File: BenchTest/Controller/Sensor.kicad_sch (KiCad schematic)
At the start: 1 part, among them J2 Conn_01x03

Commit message: WIP Controller in progress
w
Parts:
- removed J2: Conn_01x03, symbol Connector_Generic:Conn_01x03
- added J2, J4: Conn_01x04, symbol Connector_Generic:Conn_01x04
- added J3: Conn_01x03, symbol Connector_Generic:Conn_01x03
- added R11, R12: 10k, Resistor_SMD:R_0402_1005Metric_Pad0.72x0.64mm_HandSolder, symbol Device:R
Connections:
- net GND: now also J2.3 (Pin_3), J4.4 (Pin_4), R12.2
- net Sense: now also J2.2 (Pin_2)
- new net +5V: J2.4 (Pin_4)
- new net CurentSenseVRef: J2.1 (Pin_1)
- new net PEDAL_OUT: J4.1 (Pin_1), R11.1
- new net PEDAL_SWITCH_0: J4.2 (Pin_2)
- new net PEDAL_SWITCH_1: J4.3 (Pin_3)
- new net Pedal_Signal: R11.2, R12.1
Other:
- note added: "TODO Pedal Connection TODO what is the voltage TODO divide it down? TODO use op-amp for faster slew?"
- note added: "TODO Pedal This signal goes to 3 different controllers. Howdo."
- note added: "TODO expected ~25mA. Switch?"
- note added: "TODO need 2.5V Reference, but able to supply 5mA. Need an LDO here TODO halve Sense? Sensor is hass-200"
- note added: "TODO thermal from motor"
- note removed: "TODO Pinout TODO what is the drive from the current sensor TODO what is the voltage"

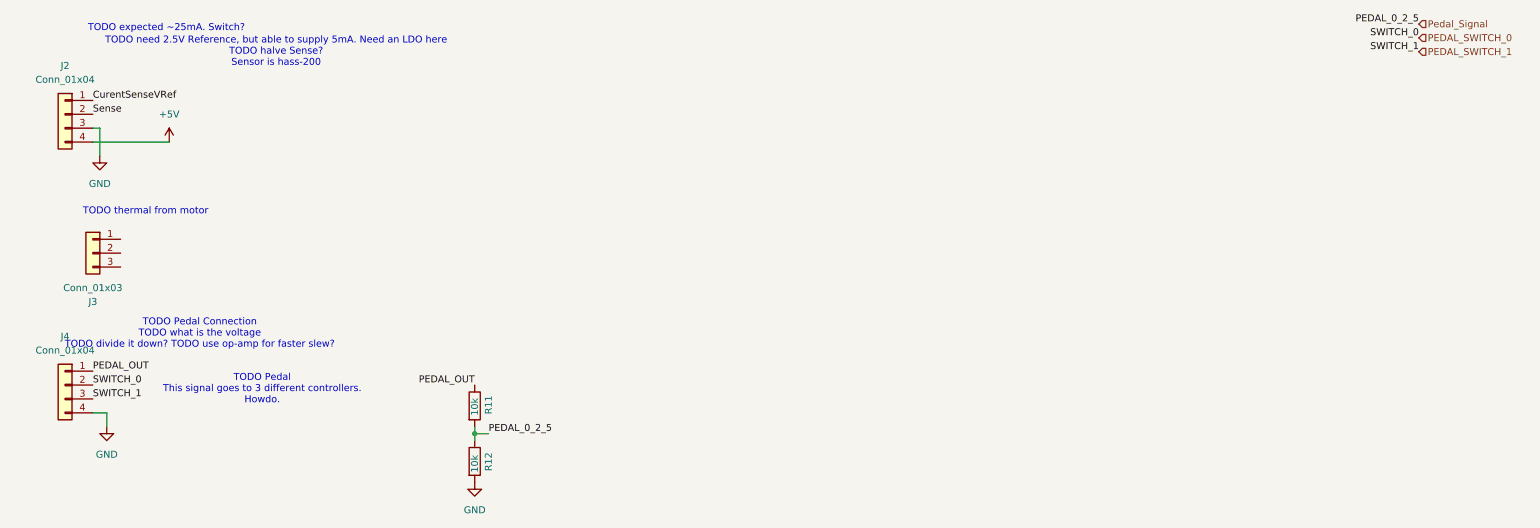
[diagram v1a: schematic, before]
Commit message: Migrated to 5V drive from digital side
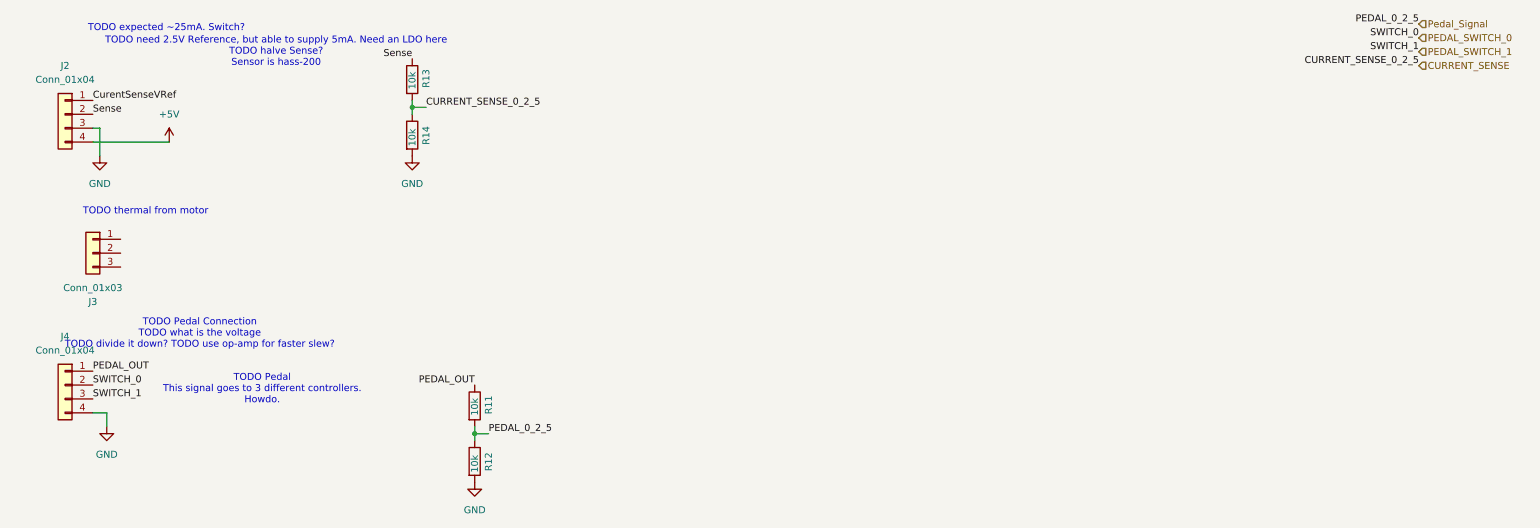
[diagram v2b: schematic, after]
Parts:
- added R13, R14: 10k, Resistor_SMD:R_0402_1005Metric_Pad0.72x0.64mm_HandSolder, symbol Device:R
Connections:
- net GND: now also R14.2
- net Sense: now also R13.1
- new net CURRENT_SENSE: R13.2, R14.1
